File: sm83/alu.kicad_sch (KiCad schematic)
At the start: 34 parts

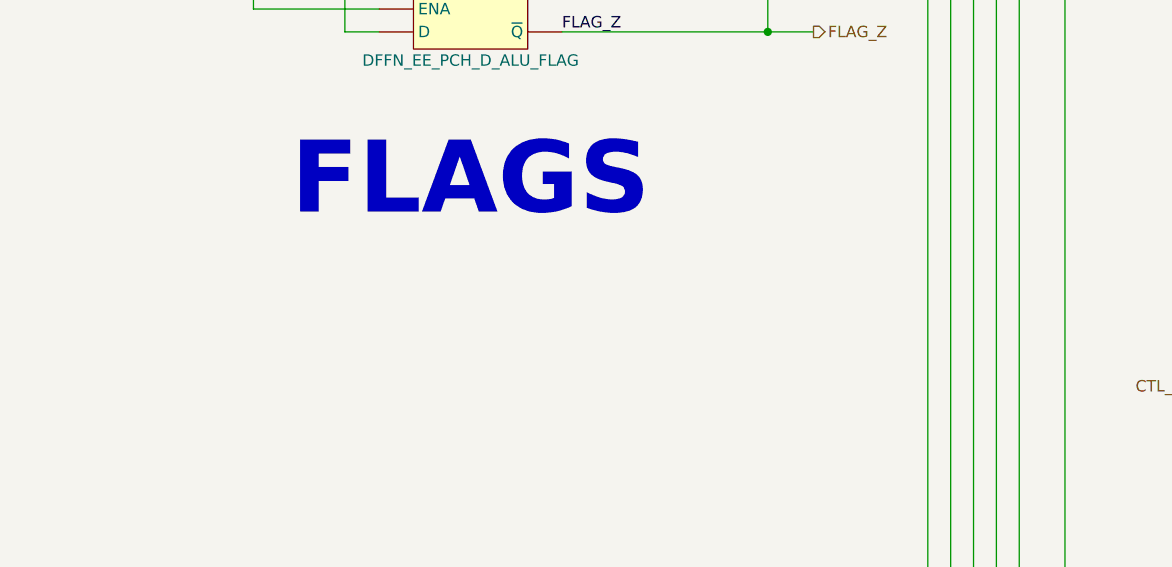
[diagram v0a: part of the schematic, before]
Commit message: SM83: Add data bus bridge schematic
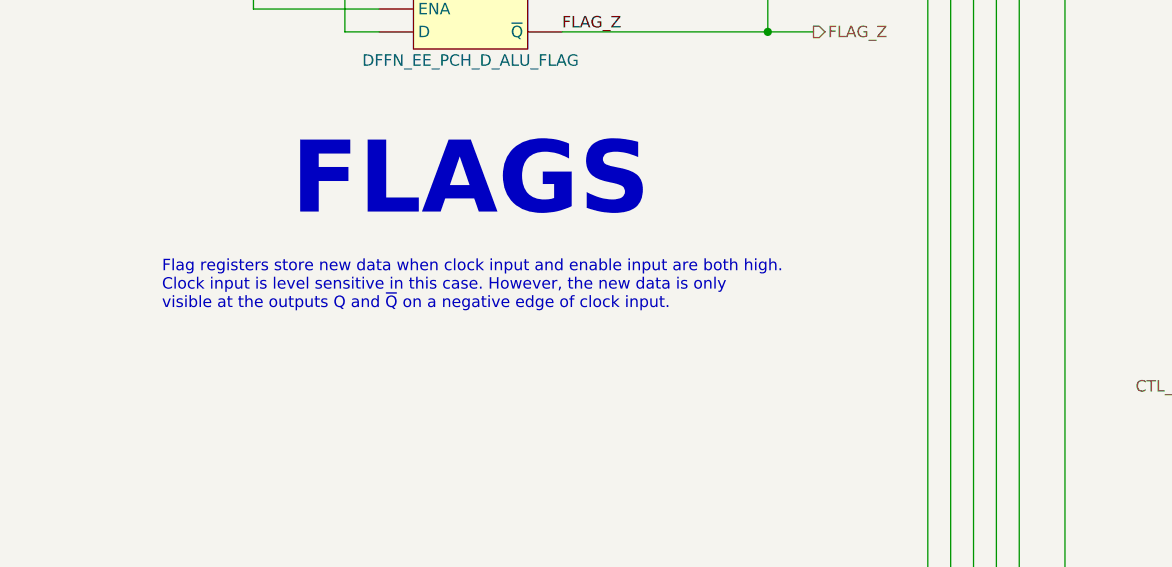
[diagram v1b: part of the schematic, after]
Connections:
- new net: ALU_AND6.2, ALU_CGGEN_H. (COUT0), ALU_PGGEN6. (Y)
- new net: ALU_AND2.2, ALU_CGGEN_L. (COUT0), ALU_PGGEN2. (Y)
- new net: ALU_CGGEN_L. (COUT0), ALU_PGGEN2. (Y)
- new net: ALU_PGGEN2. (Y), ALU_SHIFTER. (Y2)
- new net: ALU_CGGEN_H. (COUT0), ALU_PGGEN4. (Y)
- new net: ALU_AND4.1, ALU_CGGEN_H. (COUT0), ALU_PGGEN4. (Y)
- new net: ALU_PGGEN4. (Y), ALU_SHIFTER. (Y4)
- new net: ALU_CGGEN_H. (COUT0), ALU_PGGEN6. (Y)
- new net: ALU_CGGEN_H. (COUT0), ALU_PGGEN7. (Y)
- new net: ALU_AND7.1, ALU_CGGEN_H. (COUT0), ALU_PGGEN7. (Y)
- new net: ALU_AND5.2, ALU_CGGEN_H. (COUT0), ALU_PGGEN5. (Y)
- new net: ALU_CGGEN_H. (COUT0), ALU_PGGEN5. (Y)
- new net: ALU_AND3.2, ALU_CGGEN_L. (COUT0), ALU_PGGEN3. (Y)
- new net: ALU_PGGEN6. (Y), ALU_SHIFTER. (Y6)
- new net: ALU_CGGEN_L. (COUT0), ALU_PGGEN0. (Y)
- new net: ALU_AND0.1, ALU_CGGEN_L. (COUT0), ALU_PGGEN0. (Y)
- new net: ALU_AND1.2, ALU_CGGEN_L. (COUT0), ALU_PGGEN1. (Y)
- new net: ALU_CGGEN_L. (COUT0), ALU_PGGEN1. (Y)
- new net: ALU_CGGEN_L. (COUT0), ALU_PGGEN3. (Y)
- new net: ALU_PGGEN0. (Y), ALU_SHIFTER. (Y0)
- new net: ALU_PGGEN7. (Y), ALU_SHIFTER. (Y7)
- new net: ALU_PGGEN5. (Y), ALU_SHIFTER. (Y5)
- new net: ALU_PGGEN1. (Y), ALU_SHIFTER. (Y1)
- new net: ALU_PGGEN3. (Y), ALU_SHIFTER. (Y3)
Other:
- note added: "Flag registers store new data when clock input and enable input are both high. Clock input is level sensitive in this case. However, the new data is only visible at the outputs Q and ~{Q} on a negative edge of clock input."
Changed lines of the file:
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@@
+		)
+	)
+	(text "Flag registers store new data when clock input and enable input are both high.\nClock input is level sensitive in this case. However, the new data is only\nvisible at the outputs Q and ~{Q} on a negative edge of clock input."
+		(exclude_from_sim no)
+		(at 134.62 468.63 0)
+		(effects
+			(font
+				(size 1.27 1.27)
+			)
+			(justify left top)
 		)
 	)

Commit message: Finish SM83 CPU schematic
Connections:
- new net: ALU_AND6.2, ALU_CGGEN_H. (COUT0), ALU_PGGEN6. (Y)
- new net: ALU_AND2.2, ALU_CGGEN_L. (COUT0), ALU_PGGEN2. (Y)
- new net: ALU_CGGEN_L. (COUT0), ALU_PGGEN2. (Y)
- new net: ALU_PGGEN2. (Y), ALU_SHIFTER. (Y2)
- new net: ALU_CGGEN_H. (COUT0), ALU_PGGEN4. (Y)
- new net: ALU_AND4.1, ALU_CGGEN_H. (COUT0), ALU_PGGEN4. (Y)
- new net: ALU_PGGEN4. (Y), ALU_SHIFTER. (Y4)
- new net: ALU_CGGEN_H. (COUT0), ALU_PGGEN6. (Y)
- new net: ALU_CGGEN_H. (COUT0), ALU_PGGEN7. (Y)
- new net: ALU_AND7.1, ALU_CGGEN_H. (COUT0), ALU_PGGEN7. (Y)
- new net: ALU_AND5.2, ALU_CGGEN_H. (COUT0), ALU_PGGEN5. (Y)
- new net: ALU_CGGEN_H. (COUT0), ALU_PGGEN5. (Y)
- new net: ALU_AND3.2, ALU_CGGEN_L. (COUT0), ALU_PGGEN3. (Y)
- new net: ALU_PGGEN6. (Y), ALU_SHIFTER. (Y6)
- new net: ALU_CGGEN_L. (COUT0), ALU_PGGEN0. (Y)
- new net: ALU_AND0.1, ALU_CGGEN_L. (COUT0), ALU_PGGEN0. (Y)
- new net: ALU_AND1.2, ALU_CGGEN_L. (COUT0), ALU_PGGEN1. (Y)
- new net: ALU_CGGEN_L. (COUT0), ALU_PGGEN1. (Y)
- new net: ALU_CGGEN_L. (COUT0), ALU_PGGEN3. (Y)
- new net: ALU_PGGEN0. (Y), ALU_SHIFTER. (Y0)
- new net: ALU_PGGEN7. (Y), ALU_SHIFTER. (Y7)
- new net: ALU_PGGEN5. (Y), ALU_SHIFTER. (Y5)
- new net: ALU_PGGEN1. (Y), ALU_SHIFTER. (Y1)
- new net: ALU_PGGEN3. (Y), ALU_SHIFTER. (Y3)
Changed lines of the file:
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@@
 	(title_block
 		(title "SM83 CPU")
-		(date "2025-12-08")
+		(date "2025-12-24")
 		(rev "0")
 		(company "CC-BY-SA-4.0 Michael Singer")

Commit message: SM83: Merge dist. NANDs and NOR from IRQ_PRIOs
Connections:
- new net: ALU_AND6.2, ALU_CGGEN_H. (COUT0), ALU_PGGEN6. (Y)
- new net: ALU_AND2.2, ALU_CGGEN_L. (COUT0), ALU_PGGEN2. (Y)
- new net: ALU_CGGEN_L. (COUT0), ALU_PGGEN2. (Y)
- new net: ALU_PGGEN2. (Y), ALU_SHIFTER. (Y2)
- new net: ALU_CGGEN_H. (COUT0), ALU_PGGEN4. (Y)
- new net: ALU_AND4.1, ALU_CGGEN_H. (COUT0), ALU_PGGEN4. (Y)
- new net: ALU_PGGEN4. (Y), ALU_SHIFTER. (Y4)
- new net: ALU_CGGEN_H. (COUT0), ALU_PGGEN6. (Y)
- new net: ALU_CGGEN_H. (COUT0), ALU_PGGEN7. (Y)
- new net: ALU_AND7.1, ALU_CGGEN_H. (COUT0), ALU_PGGEN7. (Y)
- new net: ALU_AND5.2, ALU_CGGEN_H. (COUT0), ALU_PGGEN5. (Y)
- new net: ALU_CGGEN_H. (COUT0), ALU_PGGEN5. (Y)
- new net: ALU_AND3.2, ALU_CGGEN_L. (COUT0), ALU_PGGEN3. (Y)
- new net: ALU_PGGEN6. (Y), ALU_SHIFTER. (Y6)
- new net: ALU_CGGEN_L. (COUT0), ALU_PGGEN0. (Y)
- new net: ALU_AND0.1, ALU_CGGEN_L. (COUT0), ALU_PGGEN0. (Y)
- new net: ALU_AND1.2, ALU_CGGEN_L. (COUT0), ALU_PGGEN1. (Y)
- new net: ALU_CGGEN_L. (COUT0), ALU_PGGEN1. (Y)
- new net: ALU_CGGEN_L. (COUT0), ALU_PGGEN3. (Y)
- new net: ALU_PGGEN0. (Y), ALU_SHIFTER. (Y0)
- new net: ALU_PGGEN7. (Y), ALU_SHIFTER. (Y7)
- new net: ALU_PGGEN5. (Y), ALU_SHIFTER. (Y5)
- new net: ALU_PGGEN1. (Y), ALU_SHIFTER. (Y1)
- new net: ALU_PGGEN3. (Y), ALU_SHIFTER. (Y3)
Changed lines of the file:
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@@
 	(title_block
 		(title "SM83 CPU")
-		(date "2025-12-24")
+		(date "2025-12-25")
 		(rev "0")
 		(company "CC-BY-SA-4.0 Michael Singer")

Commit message: Release version 0.9 of both schematics
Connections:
- new net: ALU_AND6.2, ALU_CGGEN_H. (COUT0), ALU_PGGEN6. (Y)
- new net: ALU_AND2.2, ALU_CGGEN_L. (COUT0), ALU_PGGEN2. (Y)
- new net: ALU_CGGEN_L. (COUT0), ALU_PGGEN2. (Y)
- new net: ALU_PGGEN2. (Y), ALU_SHIFTER. (Y2)
- new net: ALU_CGGEN_H. (COUT0), ALU_PGGEN4. (Y)
- new net: ALU_AND4.1, ALU_CGGEN_H. (COUT0), ALU_PGGEN4. (Y)
- new net: ALU_PGGEN4. (Y), ALU_SHIFTER. (Y4)
- new net: ALU_CGGEN_H. (COUT0), ALU_PGGEN6. (Y)
- new net: ALU_CGGEN_H. (COUT0), ALU_PGGEN7. (Y)
- new net: ALU_AND7.1, ALU_CGGEN_H. (COUT0), ALU_PGGEN7. (Y)
- new net: ALU_AND5.2, ALU_CGGEN_H. (COUT0), ALU_PGGEN5. (Y)
- new net: ALU_CGGEN_H. (COUT0), ALU_PGGEN5. (Y)
- new net: ALU_AND3.2, ALU_CGGEN_L. (COUT0), ALU_PGGEN3. (Y)
- new net: ALU_PGGEN6. (Y), ALU_SHIFTER. (Y6)
- new net: ALU_CGGEN_L. (COUT0), ALU_PGGEN0. (Y)
- new net: ALU_AND0.1, ALU_CGGEN_L. (COUT0), ALU_PGGEN0. (Y)
- new net: ALU_AND1.2, ALU_CGGEN_L. (COUT0), ALU_PGGEN1. (Y)
- new net: ALU_CGGEN_L. (COUT0), ALU_PGGEN1. (Y)
- new net: ALU_CGGEN_L. (COUT0), ALU_PGGEN3. (Y)
- new net: ALU_PGGEN0. (Y), ALU_SHIFTER. (Y0)
- new net: ALU_PGGEN7. (Y), ALU_SHIFTER. (Y7)
- new net: ALU_PGGEN5. (Y), ALU_SHIFTER. (Y5)
- new net: ALU_PGGEN1. (Y), ALU_SHIFTER. (Y1)
- new net: ALU_PGGEN3. (Y), ALU_SHIFTER. (Y3)
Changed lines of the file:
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@@
 		(title "SM83 CPU")
 		(date "2025-12-25")
-		(rev "0")
+		(rev "0.9")
 		(company "CC-BY-SA-4.0 Michael Singer")
 		(comment 1 "https://github.com/msinger/dmg-schematics")

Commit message: Release revision 0.10 of both schematics
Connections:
- new net: ALU_AND6.2, ALU_CGGEN_H. (COUT0), ALU_PGGEN6. (Y)
- new net: ALU_AND2.2, ALU_CGGEN_L. (COUT0), ALU_PGGEN2. (Y)
- new net: ALU_CGGEN_L. (COUT0), ALU_PGGEN2. (Y)
- new net: ALU_PGGEN2. (Y), ALU_SHIFTER. (Y2)
- new net: ALU_CGGEN_H. (COUT0), ALU_PGGEN4. (Y)
- new net: ALU_AND4.1, ALU_CGGEN_H. (COUT0), ALU_PGGEN4. (Y)
- new net: ALU_PGGEN4. (Y), ALU_SHIFTER. (Y4)
- new net: ALU_CGGEN_H. (COUT0), ALU_PGGEN6. (Y)
- new net: ALU_CGGEN_H. (COUT0), ALU_PGGEN7. (Y)
- new net: ALU_AND7.1, ALU_CGGEN_H. (COUT0), ALU_PGGEN7. (Y)
- new net: ALU_AND5.2, ALU_CGGEN_H. (COUT0), ALU_PGGEN5. (Y)
- new net: ALU_CGGEN_H. (COUT0), ALU_PGGEN5. (Y)
- new net: ALU_AND3.2, ALU_CGGEN_L. (COUT0), ALU_PGGEN3. (Y)
- new net: ALU_PGGEN6. (Y), ALU_SHIFTER. (Y6)
- new net: ALU_CGGEN_L. (COUT0), ALU_PGGEN0. (Y)
- new net: ALU_AND0.1, ALU_CGGEN_L. (COUT0), ALU_PGGEN0. (Y)
- new net: ALU_AND1.2, ALU_CGGEN_L. (COUT0), ALU_PGGEN1. (Y)
- new net: ALU_CGGEN_L. (COUT0), ALU_PGGEN1. (Y)
- new net: ALU_CGGEN_L. (COUT0), ALU_PGGEN3. (Y)
- new net: ALU_PGGEN0. (Y), ALU_SHIFTER. (Y0)
- new net: ALU_PGGEN7. (Y), ALU_SHIFTER. (Y7)
- new net: ALU_PGGEN5. (Y), ALU_SHIFTER. (Y5)
- new net: ALU_PGGEN1. (Y), ALU_SHIFTER. (Y1)
- new net: ALU_PGGEN3. (Y), ALU_SHIFTER. (Y3)
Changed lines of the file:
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@@
 	(title_block
 		(title "SM83 CPU")
-		(date "2025-12-25")
-		(rev "0.9")
+		(date "2026-03-22")
+		(rev "0.10")
 		(company "CC-BY-SA-4.0 Michael Singer")
 		(comment 1 "https://github.com/msinger/dmg-schematics")
@@
 		)
 		(instances
-			(project ""
+			(project "sm83"
 				(path "/8717d046-1dfd-46fe-a5f7-4e4d2f07de68/ab5e4a9c-ae63-4ff1-a186-b2eaad3dc19d"
 					(reference "ALU_RESULT0")
@@
 		)
 		(instances
-			(project ""
+			(project "sm83"
 				(path "/8717d046-1dfd-46fe-a5f7-4e4d2f07de68/ab5e4a9c-ae63-4ff1-a186-b2eaad3dc19d"
 					(reference "ALU_SHIFTER")
@@
 		)
 		(instances
-			(project ""
+			(project "sm83"
 				(path "/8717d046-1dfd-46fe-a5f7-4e4d2f07de68/ab5e4a9c-ae63-4ff1-a186-b2eaad3dc19d"
 					(reference "ALU_CGGEN_L")
@@
 		)
 		(instances
-			(project ""
+			(project "sm83"
 				(path "/8717d046-1dfd-46fe-a5f7-4e4d2f07de68/ab5e4a9c-ae63-4ff1-a186-b2eaad3dc19d"
 					(reference "ALU_PGGEN0")
@@
 		)
 		(instances
-			(project ""
+			(project "sm83"
 				(path "/8717d046-1dfd-46fe-a5f7-4e4d2f07de68/ab5e4a9c-ae63-4ff1-a186-b2eaad3dc19d"
 					(reference "ALU_NOT11")
@@
 		)
 		(instances
-			(project ""
+			(project "sm83"
 				(path "/8717d046-1dfd-46fe-a5f7-4e4d2f07de68/ab5e4a9c-ae63-4ff1-a186-b2eaad3dc19d"
 					(reference "ALU_SHIFTER")
@@
 		)
 		(instances
-			(project ""
+			(project "sm83"
 				(path "/8717d046-1dfd-46fe-a5f7-4e4d2f07de68/ab5e4a9c-ae63-4ff1-a186-b2eaad3dc19d"
 					(reference "ALU_SHIFTER")
@@
 		)
 		(instances
-			(project ""
+			(project "sm83"
 				(path "/8717d046-1dfd-46fe-a5f7-4e4d2f07de68/ab5e4a9c-ae63-4ff1-a186-b2eaad3dc19d"
 					(reference "ALU_SHIFTER")
@@
 		)
 		(instances
-			(project ""
+			(project "sm83"
 				(path "/8717d046-1dfd-46fe-a5f7-4e4d2f07de68/ab5e4a9c-ae63-4ff1-a186-b2eaad3dc19d"
 					(reference "ALU_ZGEN")
@@
 		)
 		(instances
-			(project ""
+			(project "sm83"
 				(path "/8717d046-1dfd-46fe-a5f7-4e4d2f07de68/ab5e4a9c-ae63-4ff1-a186-b2eaad3dc19d"
 					(reference "ALU_SHIFTER")
@@
 		)
 		(instances
-			(project ""
+			(project "sm83"
 				(path "/8717d046-1dfd-46fe-a5f7-4e4d2f07de68/ab5e4a9c-ae63-4ff1-a186-b2eaad3dc19d"
 					(reference "ALU_SHIFTER")
@@
 		)
 		(instances
-			(project ""
+			(project "sm83"
 				(path "/8717d046-1dfd-46fe-a5f7-4e4d2f07de68/ab5e4a9c-ae63-4ff1-a186-b2eaad3dc19d"
 					(reference "ALU_NOT12")
@@
 		)
 		(instances
-			(project ""
+			(project "sm83"
 				(path "/8717d046-1dfd-46fe-a5f7-4e4d2f07de68/ab5e4a9c-ae63-4ff1-a186-b2eaad3dc19d"
 					(reference "FLAG_C")
@@
 		)
 		(instances
-			(project ""
+			(project "sm83"
 				(path "/8717d046-1dfd-46fe-a5f7-4e4d2f07de68/ab5e4a9c-ae63-4ff1-a186-b2eaad3dc19d"
 					(reference "ALU_SHIFTER")
@@
 		)
 		(instances
-			(project ""
+			(project "sm83"
 				(path "/8717d046-1dfd-46fe-a5f7-4e4d2f07de68/ab5e4a9c-ae63-4ff1-a186-b2eaad3dc19d"
 					(reference "ALU_AND0")
@@
 		)
 		(instances
-			(project ""
+			(project "sm83"
 				(path "/8717d046-1dfd-46fe-a5f7-4e4d2f07de68/ab5e4a9c-ae63-4ff1-a186-b2eaad3dc19d"
 					(reference "ALU_SHIFTER")

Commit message: Release revision 0.11 of both schematics
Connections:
- new net: ALU_AND6.2, ALU_CGGEN_H. (COUT0), ALU_PGGEN6. (Y)
- new net: ALU_AND2.2, ALU_CGGEN_L. (COUT0), ALU_PGGEN2. (Y)
- new net: ALU_CGGEN_L. (COUT0), ALU_PGGEN2. (Y)
- new net: ALU_PGGEN2. (Y), ALU_SHIFTER. (Y2)
- new net: ALU_CGGEN_H. (COUT0), ALU_PGGEN4. (Y)
- new net: ALU_AND4.1, ALU_CGGEN_H. (COUT0), ALU_PGGEN4. (Y)
- new net: ALU_PGGEN4. (Y), ALU_SHIFTER. (Y4)
- new net: ALU_CGGEN_H. (COUT0), ALU_PGGEN6. (Y)
- new net: ALU_CGGEN_H. (COUT0), ALU_PGGEN7. (Y)
- new net: ALU_AND7.1, ALU_CGGEN_H. (COUT0), ALU_PGGEN7. (Y)
- new net: ALU_AND5.2, ALU_CGGEN_H. (COUT0), ALU_PGGEN5. (Y)
- new net: ALU_CGGEN_H. (COUT0), ALU_PGGEN5. (Y)
- new net: ALU_AND3.2, ALU_CGGEN_L. (COUT0), ALU_PGGEN3. (Y)
- new net: ALU_PGGEN6. (Y), ALU_SHIFTER. (Y6)
- new net: ALU_CGGEN_L. (COUT0), ALU_PGGEN0. (Y)
- new net: ALU_AND0.1, ALU_CGGEN_L. (COUT0), ALU_PGGEN0. (Y)
- new net: ALU_AND1.2, ALU_CGGEN_L. (COUT0), ALU_PGGEN1. (Y)
- new net: ALU_CGGEN_L. (COUT0), ALU_PGGEN1. (Y)
- new net: ALU_CGGEN_L. (COUT0), ALU_PGGEN3. (Y)
- new net: ALU_PGGEN0. (Y), ALU_SHIFTER. (Y0)
- new net: ALU_PGGEN7. (Y), ALU_SHIFTER. (Y7)
- new net: ALU_PGGEN5. (Y), ALU_SHIFTER. (Y5)
- new net: ALU_PGGEN1. (Y), ALU_SHIFTER. (Y1)
- new net: ALU_PGGEN3. (Y), ALU_SHIFTER. (Y3)
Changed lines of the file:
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@@
 	(title_block
 		(title "SM83 CPU")
-		(date "2026-03-22")
-		(rev "0.10")
+		(date "2026-04-11")
+		(rev "0.11")
 		(company "CC-BY-SA-4.0 Michael Singer")
 		(comment 1 "https://github.com/msinger/dmg-schematics")
